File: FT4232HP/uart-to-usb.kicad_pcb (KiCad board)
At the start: 2 copper layers, 16 parts, among them J1 USB_C_Receptacle_USB2.0_16P, J2 Conn_01x05_Socket, SW1 SW_Push, U1 FT4232H, U2 AP2112K-3.3, Y1 12MHz

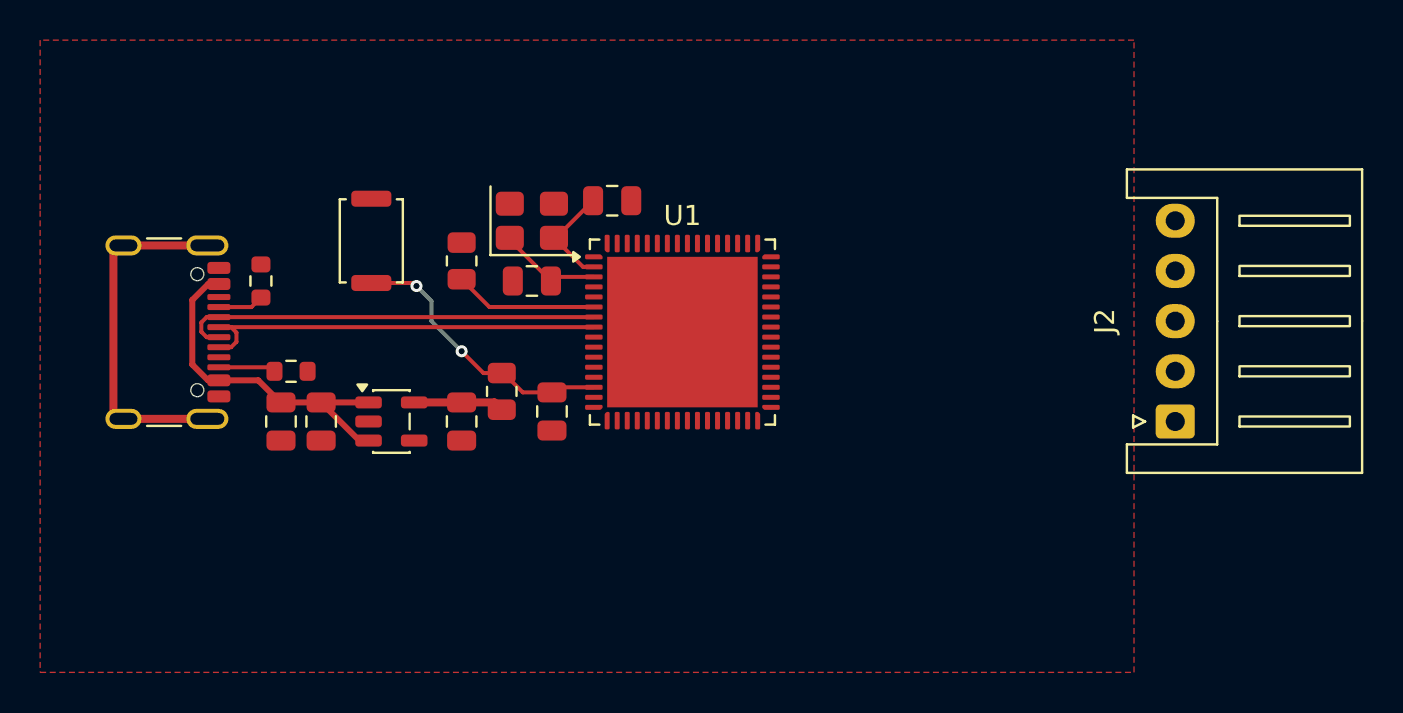
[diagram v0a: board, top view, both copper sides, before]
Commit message: Finish 4232 routing
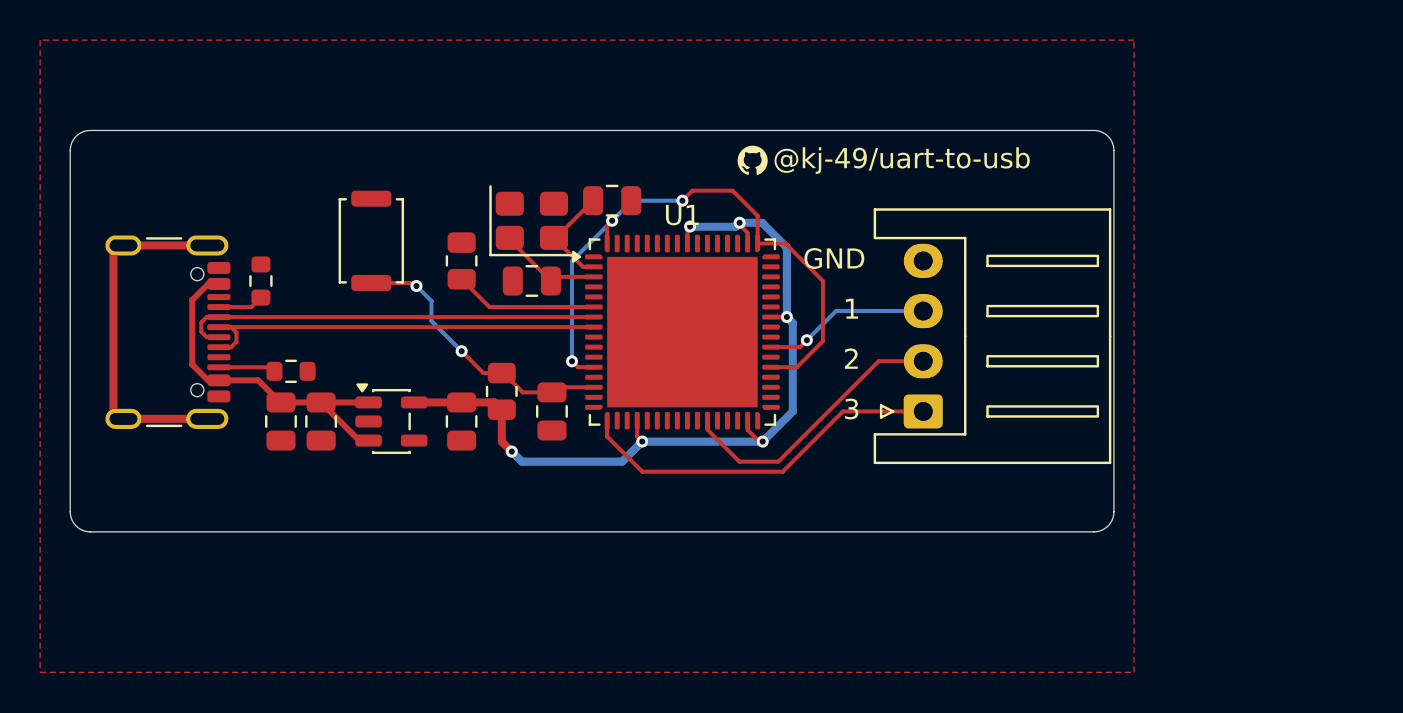
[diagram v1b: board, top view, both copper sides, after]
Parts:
- added G***: LOGO, LOGO, F.Cu at (157.5, 88.0)
- J2: value Conn_01x05_Socket -> Conn_01x04_Pin; footprint Connector_JST:JST_XH_S5B-XH-A_1x05_P2.50mm_Horizontal -> Connector_JST:JST_XH_S4B-XH-A_1x04_P2.50mm_Horizontal
- moved J2 12.6 mm to (166.0, 100.5)
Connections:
- J2 pad 4: /MCU_TX_D -> GND
- U1 pad 52: /MCU_TX_D -> unconnected-(U1-DDBUS1-Pad52)
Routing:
- net +3.3V: track 4.51 -> 41.4 mm, vias 0 -> 6
- net +1.2V: track 0.00 -> 30.2 mm, vias 0 -> 3
- net /MCU_TX_A: track 0.00 -> 18.5 mm
- net /MCU_TX_B: track 0.00 -> 13.9 mm
- net /MCU_TX_C: track 0.00 -> 8.33 mm, vias 0 -> 1
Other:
- board outline added: 52 x 20 mm
- board text added: "1"
- board text added: "2"
- board text added: "3"
- board text added: "@kj-49/uart-to-usb"
- board text added: "GND"
